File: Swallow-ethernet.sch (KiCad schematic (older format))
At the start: 25 parts, among them P1 XTAG2, P2 XMP16_TR_Link, P3 TR_Link_Out, P4 Mode_Select, U1 25MHz_ASE_CLK, U2 4k7, U3 33R, U4 33R, U5 NC7WZ07, U6 NC7WZ07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

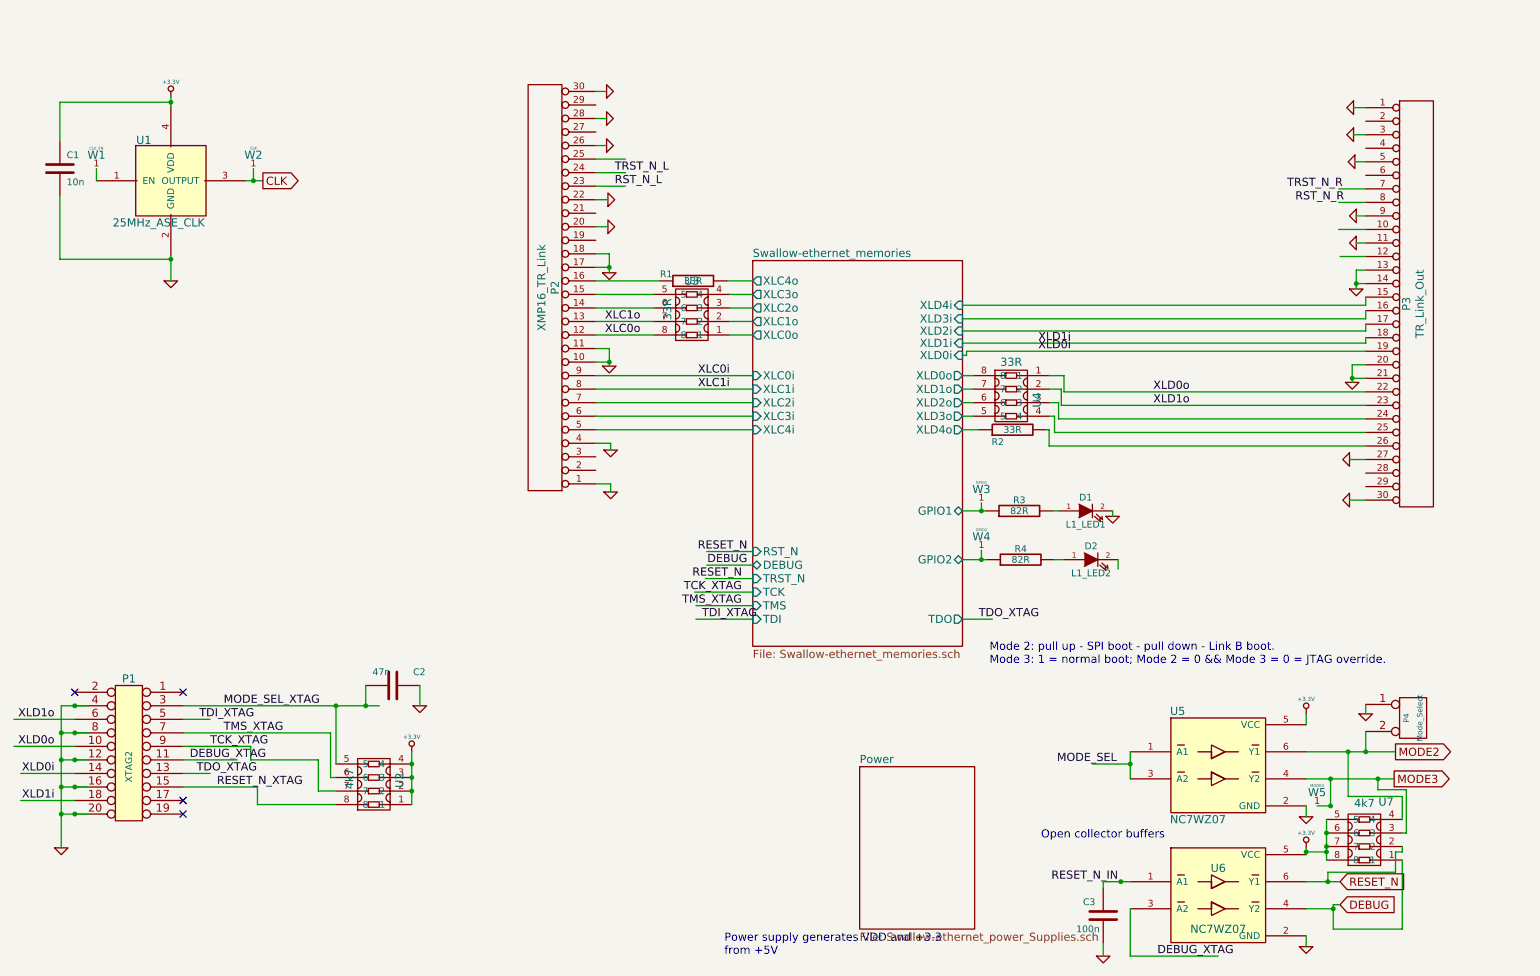
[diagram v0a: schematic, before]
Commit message: Converted LED resistors from individuals to array. Connected most signals.
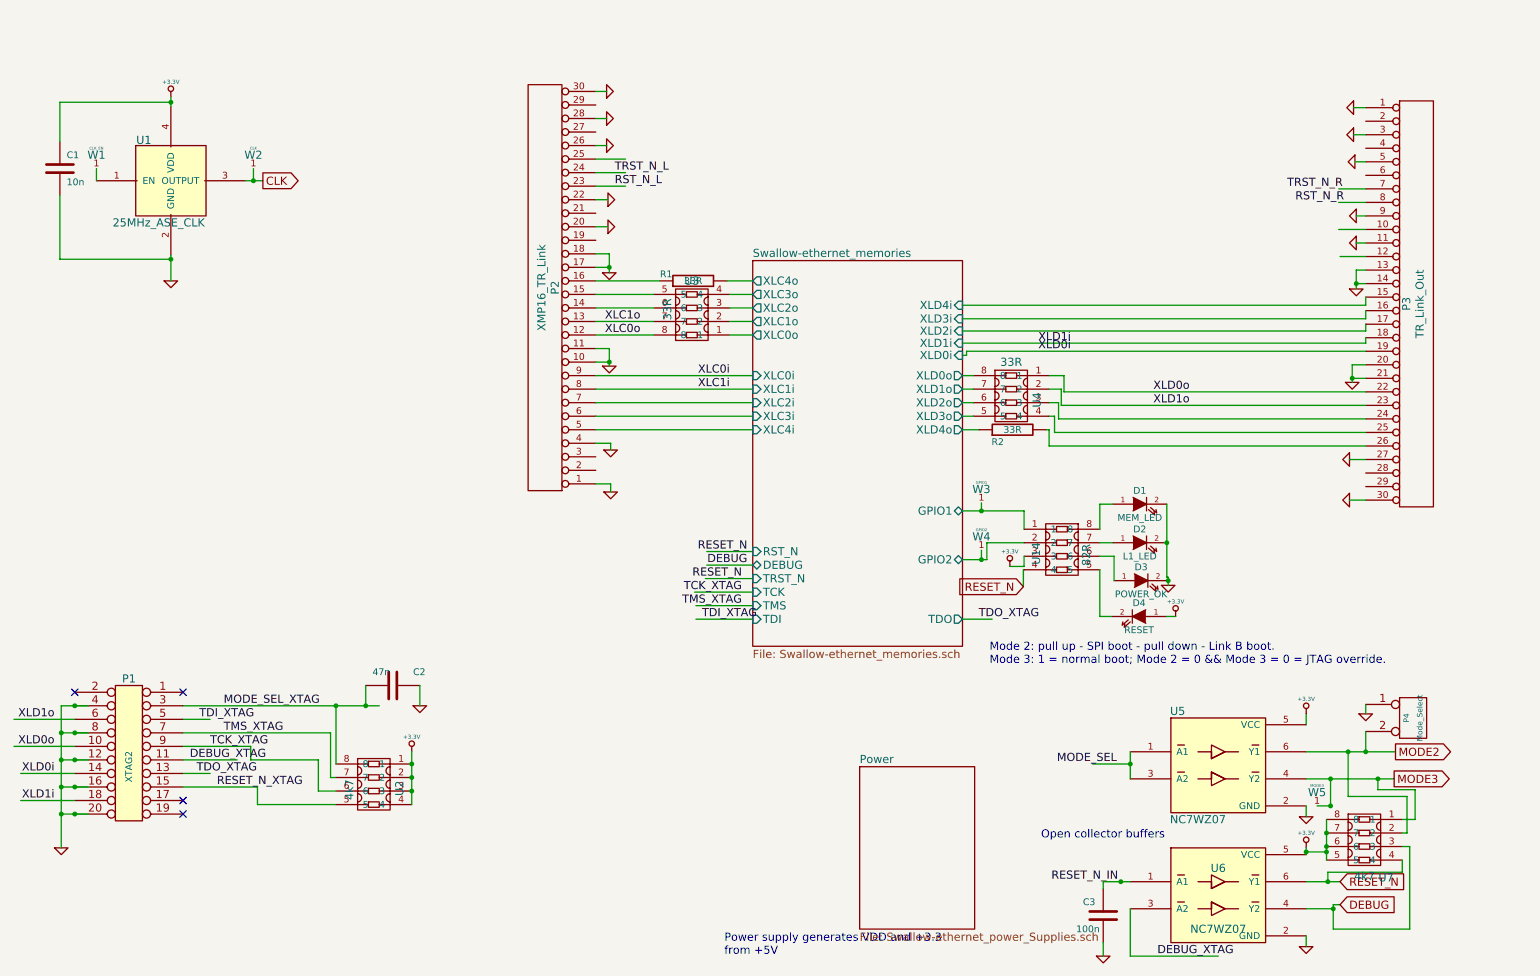
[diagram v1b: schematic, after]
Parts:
- removed R3, R4: 82R, SM0402, symbol R
- added D3: POWER_OK, X_LED-0603, symbol LED
- added D4: RESET, X_LED-0603, symbol LED
- added U14: 82R, symbol YC124
- D1: value L1_LED1 -> MEM_LED
- D2: value L1_LED2 -> L1_LED
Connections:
- wire segments 171 -> 185
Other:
- moved on the sheet: D1, D2

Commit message: Configured links to be compatible with N1, N2, S1, S2 of Swallow V2 board. Added break-out header for S1 and S2 links. Improved ground loops.
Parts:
- added P10: CONN_14, symbol CONN_14
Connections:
- net labels added: BR_P1D, BR_P1E, BR_P1H, BR_P1I, BR_P1J, BR_P1N, DEBUG_N_BL-GND_BR, GND_BL-TDI_BR, GND_BL-TDO_BR, RST_N_BL_BR, TCK_BL-GND_BR, TMS_BL-GND_BR, TRST_N_BL-GND_BR
- net labels removed: RST_N_R, TRST_N_R
- wire segments 185 -> 181
- no-connect marks 4 -> 8
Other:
- note added: "Conn to P7 or P9 on Swallow"
- note added: "Conn to Swallow P6 or P8"
- moved on the sheet: P2, P3

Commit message: Added XTAG link MUX and second breakout header to schematic.
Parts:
- added P11: CONN_8, symbol CONN_8
- added U15: 74LCX257, symbol 74LCX257
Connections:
- net labels added: XL0i_XTAG, XL0o_XTAG, XL1i_XTAG, XL1o_XTAG, XLD0i_XTAG, XLD0o_XTAG, XLD1i_XTAG, XLD1o_XTAG
- wire segments 181 -> 199
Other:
- moved on the sheet: C2, P1, U2

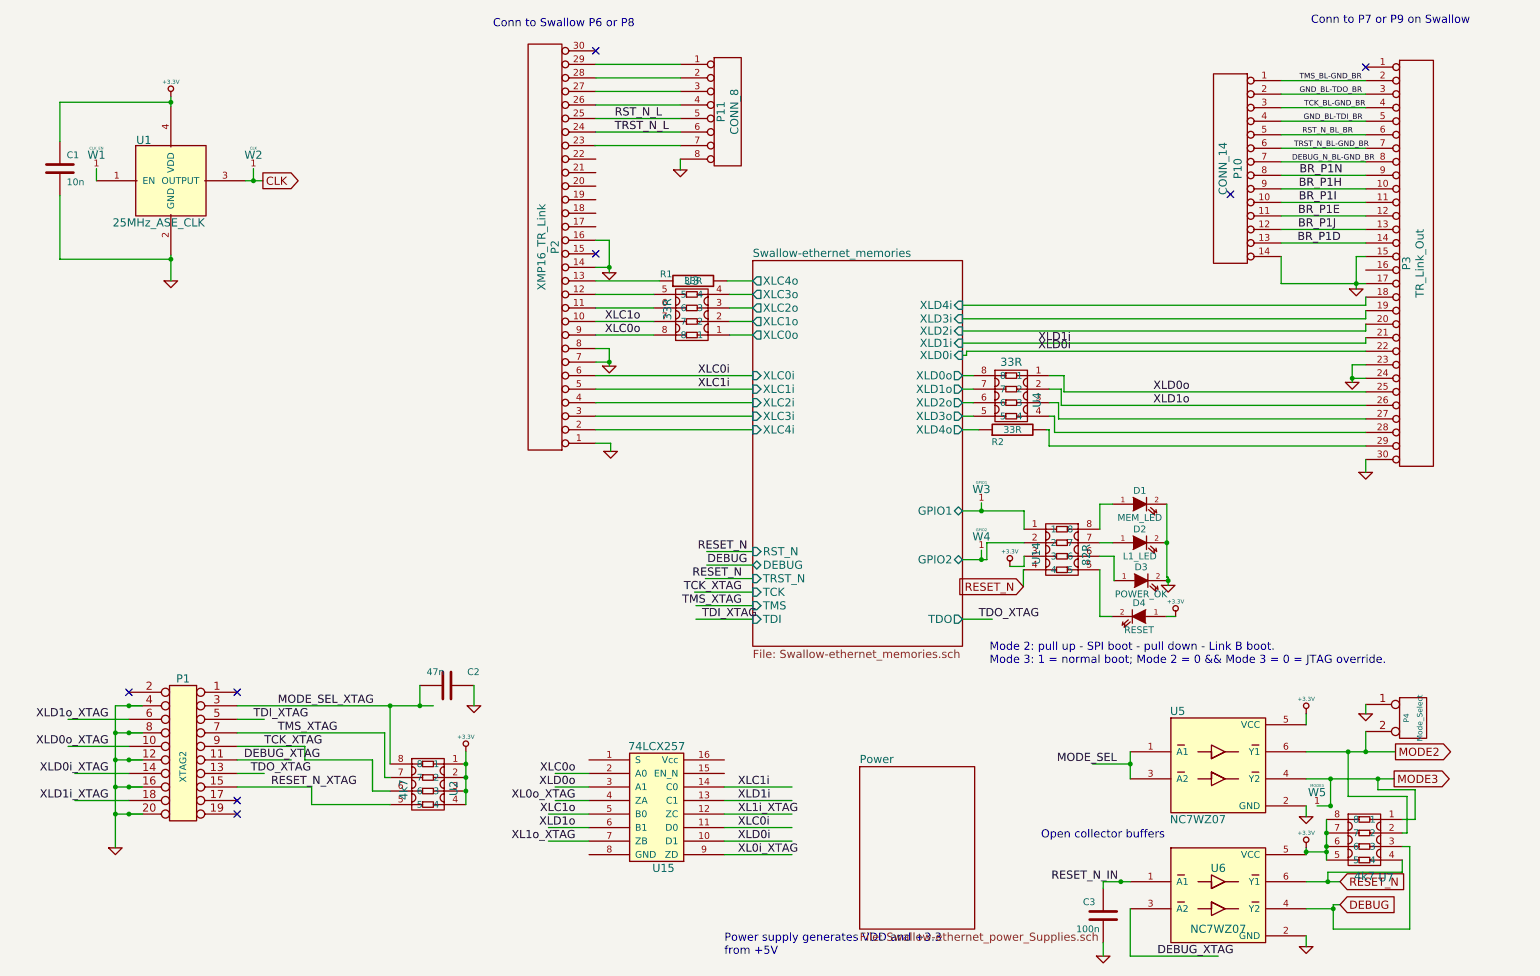
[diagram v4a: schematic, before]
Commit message: Working on making XTAG connection selectable via a MUX from either header. Tricky to route without long wiring. May reconsider or re-place.
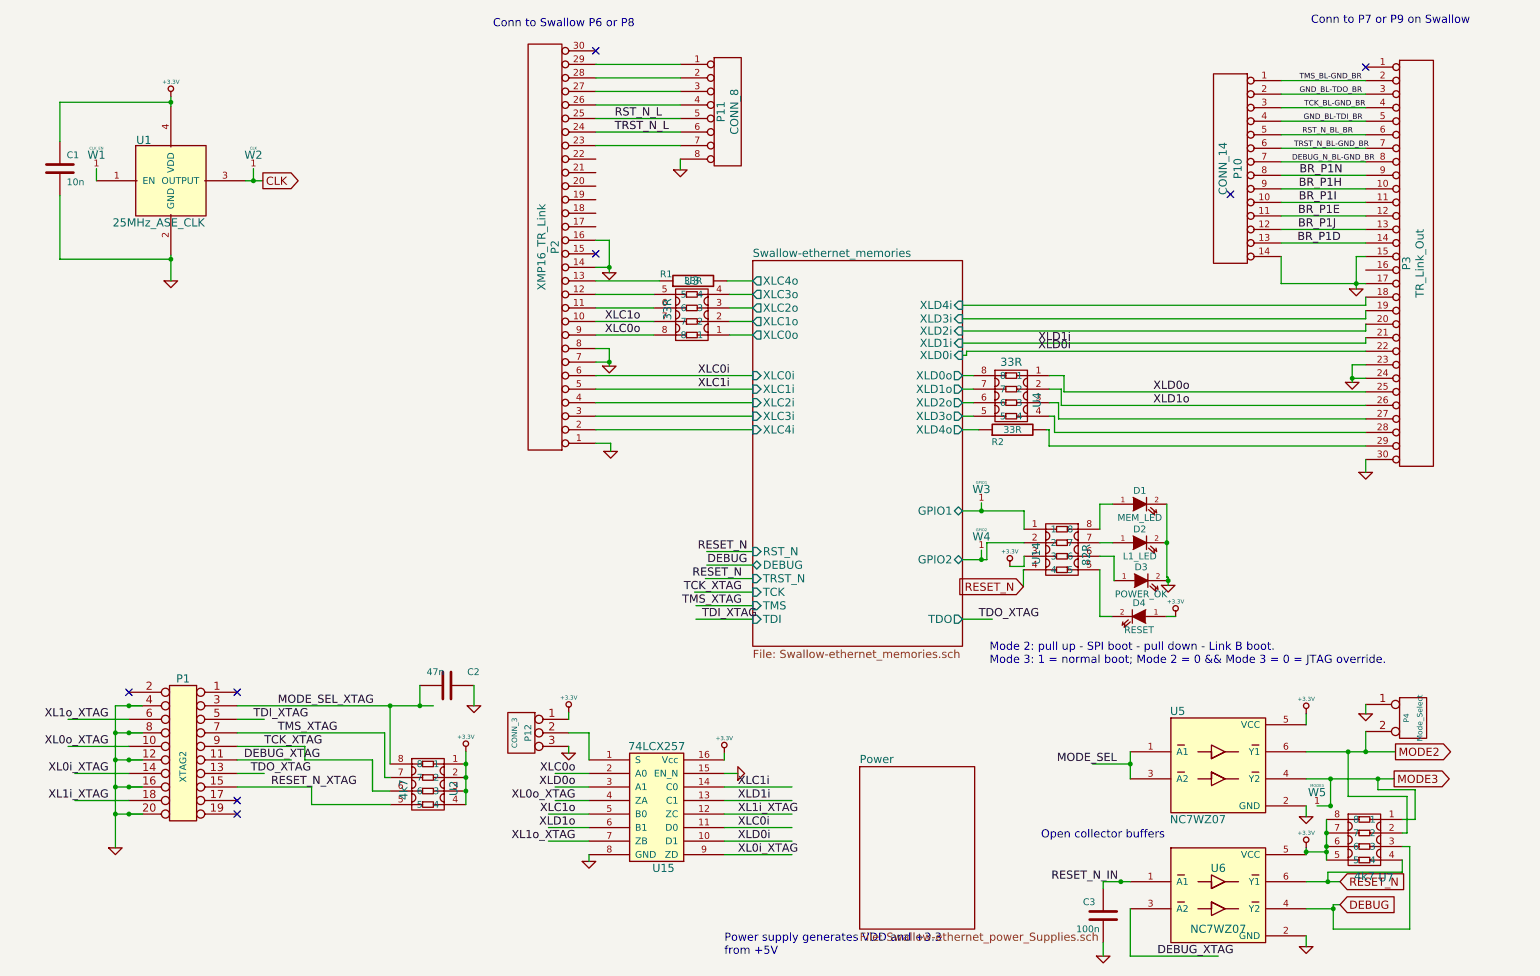
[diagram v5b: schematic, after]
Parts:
- added P12: CONN_3, symbol CONN_3
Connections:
- net labels removed: XLD0i_XTAG, XLD0o_XTAG, XLD1i_XTAG, XLD1o_XTAG
- wire segments 199 -> 206

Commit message: Completed labelling of breakout ports.
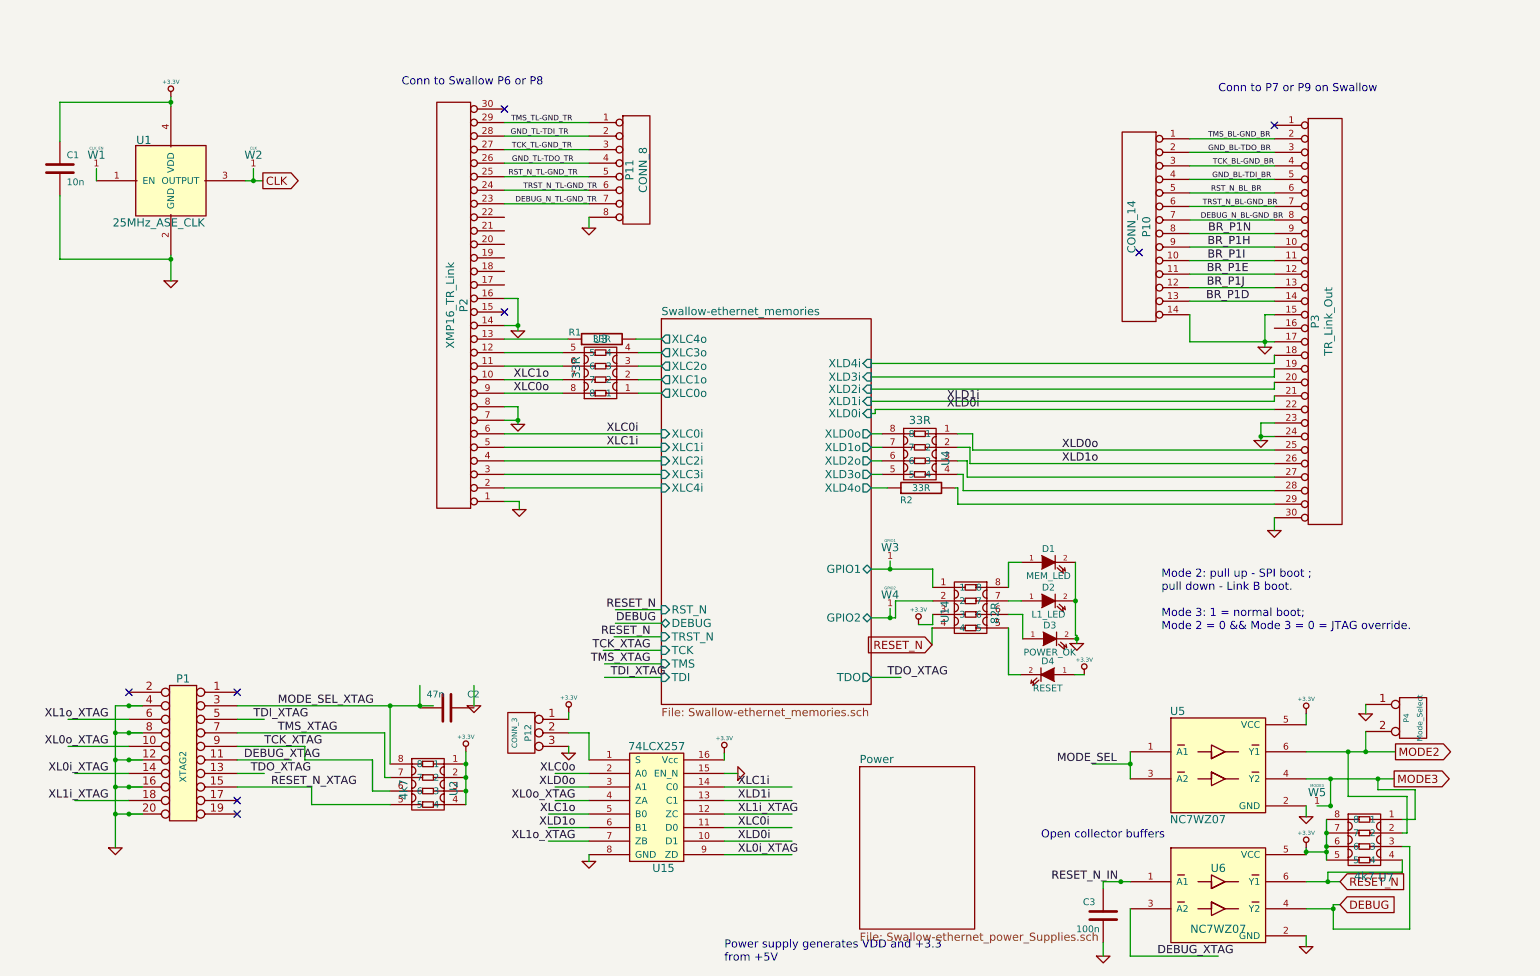
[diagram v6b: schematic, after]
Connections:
- net labels added: DEBUG_N_TL-GND_TR, GND_TL-TDI_TR, GND_TL-TDO_TR, RST_N_TL-GND_TR, TCK_TL-GND_TR, TMS_TL-GND_TR, TRST_N_TL-GND_TR
- net labels removed: RST_N_L, TRST_N_L
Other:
- note added: "Mode 2: pull up - SPI boot ;\npull down - Link B boot.\n\nMode 3: 1 = normal boot; \nMode 2 = 0 && Mode 3 = 0 = JTAG override."
- note removed: "Mode 2: pull up - SPI boot - pull down - Link B boot.\nMode 3: 1 = normal boot; Mode 2 = 0 && Mode 3 = 0 = JTAG override."
- moved on the sheet: C2, D1, D2, D3, D4, P10, P11, P2, P3, R1, R2, U14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
